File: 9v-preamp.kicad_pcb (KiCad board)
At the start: 2 copper layers, 70 x 54.5 mm, 36 parts, among them J1 GND, J2 MJ-3536, J3 Conn_01x01_Female, J4 Conn_01x01_Female, J5 Conn_01x01_Female, J6 Conn_01x01_Female, J7 Conn_01x01_Female, J8 Conn_01x01_Female, J9 Conn_01x01_Female, SW1 TE6-1A-DC-1-PB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

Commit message: Add files via upload
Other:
- board text added: "+"
- board text added: "-"

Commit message: Add files via upload
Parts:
- D1: value 2339-TLM-87G-930-S-ND -> L20697-ND
- RV1: value R_POT_TRIM-10K -> 987-1710-ND
- SW1: value TE6-1A-DC-1-PB -> 451-1158-ND
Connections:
- BT1 pad 2: GND -> V-
- C10 pad 1: GND -> V-
- C11 pad 2: GND -> V-
- C2 pad 1: GND -> V-
- C3 pad 1: GND -> V-
- C4 pad 2: GND -> V-
- C5 pad 2: GND -> V-
- C6 pad 1: GND -> V-
- C8 pad 2: GND -> V-
- D1 pad 1: GND -> V-
- D3 pad 2: GND -> V-
- J2 pad 1: GND -> V-
- J4 pad 1: GND -> V-
- R1 pad 2: GND -> V-
- R6 pad 2: GND -> V-
- RV1 pad 3: GND -> V-
- U1 pad 2: GND -> V-
- U1 pad 4: GND -> V-
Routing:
- net V-: track 0.00 -> 175.4 mm
- net GND: track 158.7 -> 0.00 mm
- net Net-(D2-Pad2): track 60.3 -> 74.3 mm
- net Net-(C10-Pad2): track 22.3 -> 34.8 mm
- net Net-(C2-Pad2): track 77.6 -> 80.7 mm
- net VCC: track 64.4 -> 67.2 mm
- net Net-(C7-Pad1): track 28.3 -> 30.9 mm
- net +out: track 32.1 -> 33.0 mm
- net Net-(C11-Pad1): track 19.5 -> 18.9 mm
- net Net-(R4-Pad2): track 32.3 -> 32.8 mm
- net Net-(R5-Pad2): track 22.8 -> 23.3 mm
- net Earth: vias 3 -> 4
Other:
- net class Default: trace_width 0.2 -> 0.8

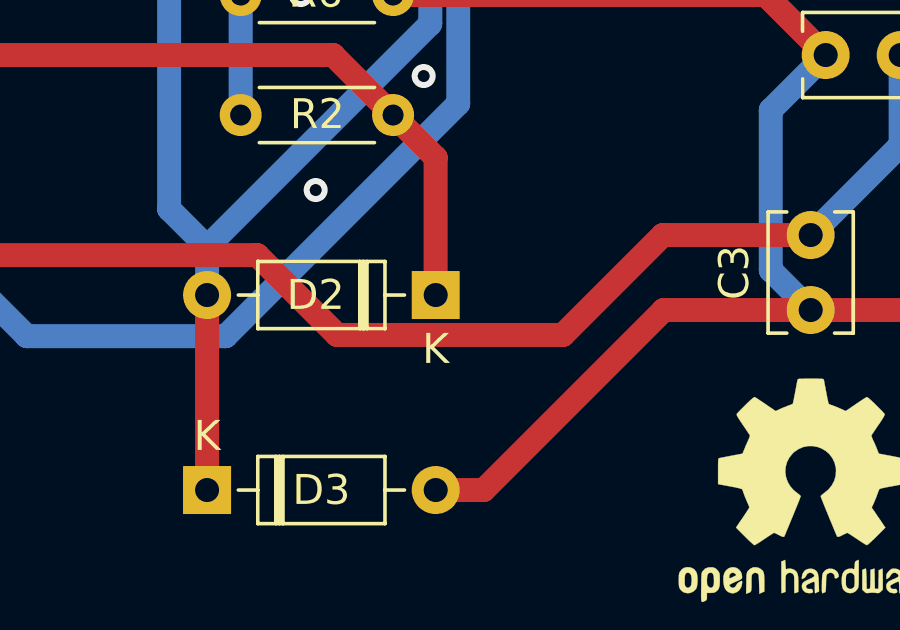
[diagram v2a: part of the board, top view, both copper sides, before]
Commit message: Add files via upload
corrected missing connection to VCC.
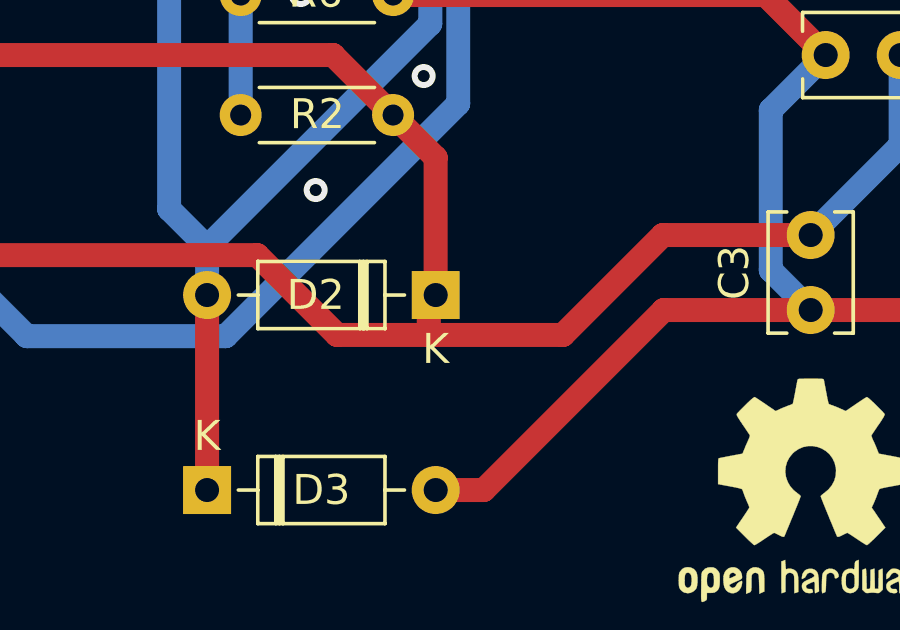
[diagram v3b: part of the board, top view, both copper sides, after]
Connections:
- C2 pad 2: Net-(C2-Pad2) -> VCC
- C3 pad 2: Net-(C2-Pad2) -> VCC
- C4 pad 1: Net-(C2-Pad2) -> VCC
- C5 pad 1: Net-(C2-Pad2) -> VCC
- C6 pad 2: Net-(C2-Pad2) -> VCC
- D1 pad 2: Net-(C2-Pad2) -> VCC
- SW1 pad 2: Net-(C2-Pad2) -> VCC
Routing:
- net VCC: track 67.2 -> 149.3 mm
- net Net-(C2-Pad2): track 80.7 -> 0.00 mm

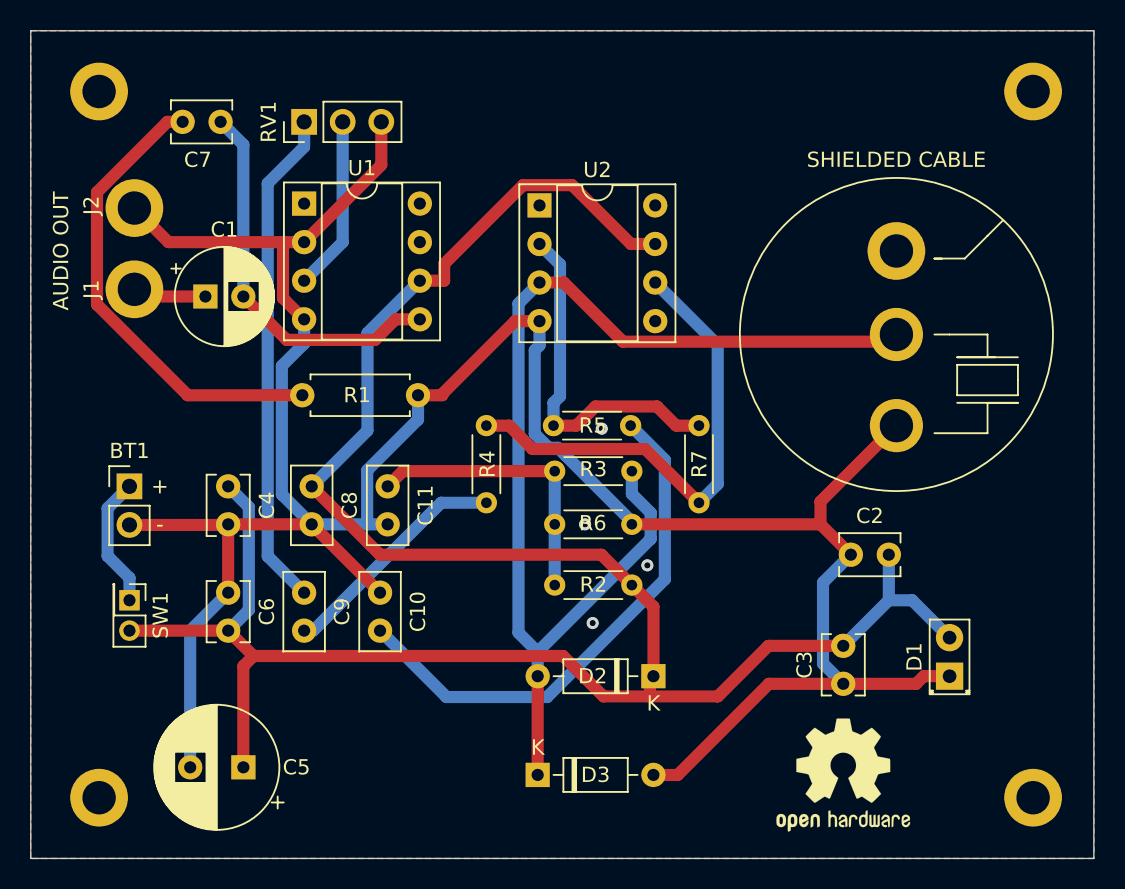
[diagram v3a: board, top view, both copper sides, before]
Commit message: Add files via upload
Added + and - marks on the LED solder connections, and pin 1 on the op amps.
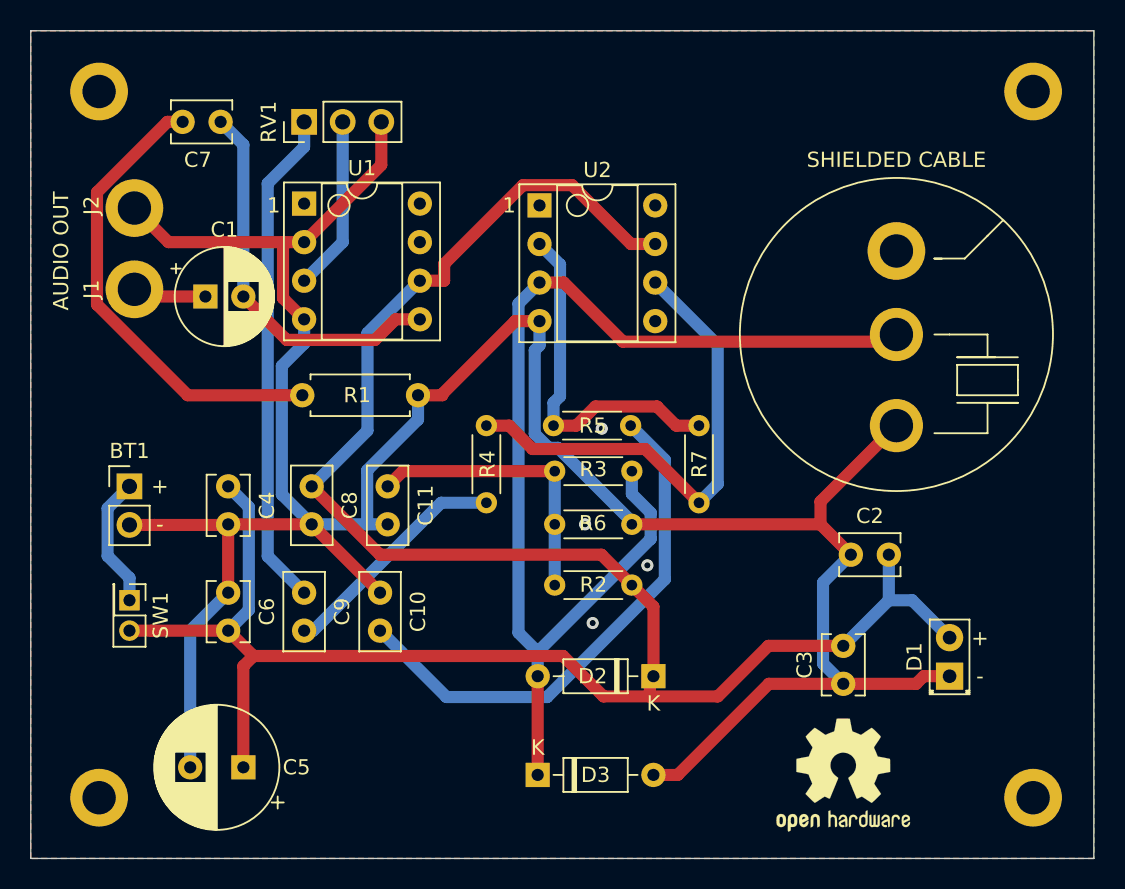
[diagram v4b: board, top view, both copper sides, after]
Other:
- board text added: "1"

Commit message: Add files via upload
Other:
- board text added: "SHIELD"
- board text added: "SLEEVE"
- board text added: "TIP"
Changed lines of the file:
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@@
   (general
     (thickness 1.6)
-    (drawings 37)
+    (drawings 40)
     (tracks 150)
     (zones 0)
@@
     (visible_elements FFFFFF7F)
     (pcbplotparams
-      (layerselection 0x010fc_ffffffff)
+      (layerselection 0x3ffff_ffffffff)
       (usegerberextensions false)
       (usegerberattributes true)
@@
     (tags "mounting hole 2.2mm m2 din965")
     (attr virtual)
-    (fp_text reference J2 (at -0.175 2.825 90) (layer F.SilkS)
+    (fp_text reference J2 (at -0.175 2.825 90) (layer F.SilkS) hide
       (effects (font (size 1 1) (thickness 0.15)))
     )
@@
     (tags "mounting hole 2.2mm m2 din965")
     (attr virtual)
-    (fp_text reference J1 (at 0 2.825 90) (layer F.SilkS)
+    (fp_text reference J1 (at 0 2.825 90) (layer F.SilkS) hide
       (effects (font (size 1 1) (thickness 0.15)))
     )
@@
     )
   )
+  (gr_text SHIELD (at 102.5 101.5) (layer F.SilkS)
+    (effects (font (size 1 1) (thickness 0.15)))
+  )
+  (gr_text SLEEVE (at 45 102.5 90) (layer F.SilkS)
+    (effects (font (size 1 1) (thickness 0.15)))
+  )
+  (gr_text TIP (at 45 97 90) (layer F.SilkS)
+    (effects (font (size 1 1) (thickness 0.15)))
+  )
   (gr_text + (at 103.5 125) (layer F.SilkS)
     (effects (font (size 1 1) (thickness 0.15)))
@@
     (connect_pads yes (clearance 0.2))
     (min_thickness 0.254)
-    (fill (arc_segments 32) (thermal_gap 0.508) (thermal_bridge_width 0.508))
+    (fill yes (arc_segments 32) (thermal_gap 0.508) (thermal_bridge_width 0.508))
     (polygon
       (pts
@@
     (connect_pads yes (clearance 0.2))
     (min_thickness 0.254)
-    (fill (arc_segments 32) (thermal_gap 0.508) (thermal_bridge_width 0.508))
+    (fill yes (arc_segments 32) (thermal_gap 0.508) (thermal_bridge_width 0.508))
     (polygon
       (pts
